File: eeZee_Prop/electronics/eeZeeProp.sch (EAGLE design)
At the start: 33 parts, among them Q1 5MHz, Q2 2N3904SMD, SW1 RESET, U1 P8X32A-Q44, U2 24LC256-I/ST, U3 NCP1117 3V3

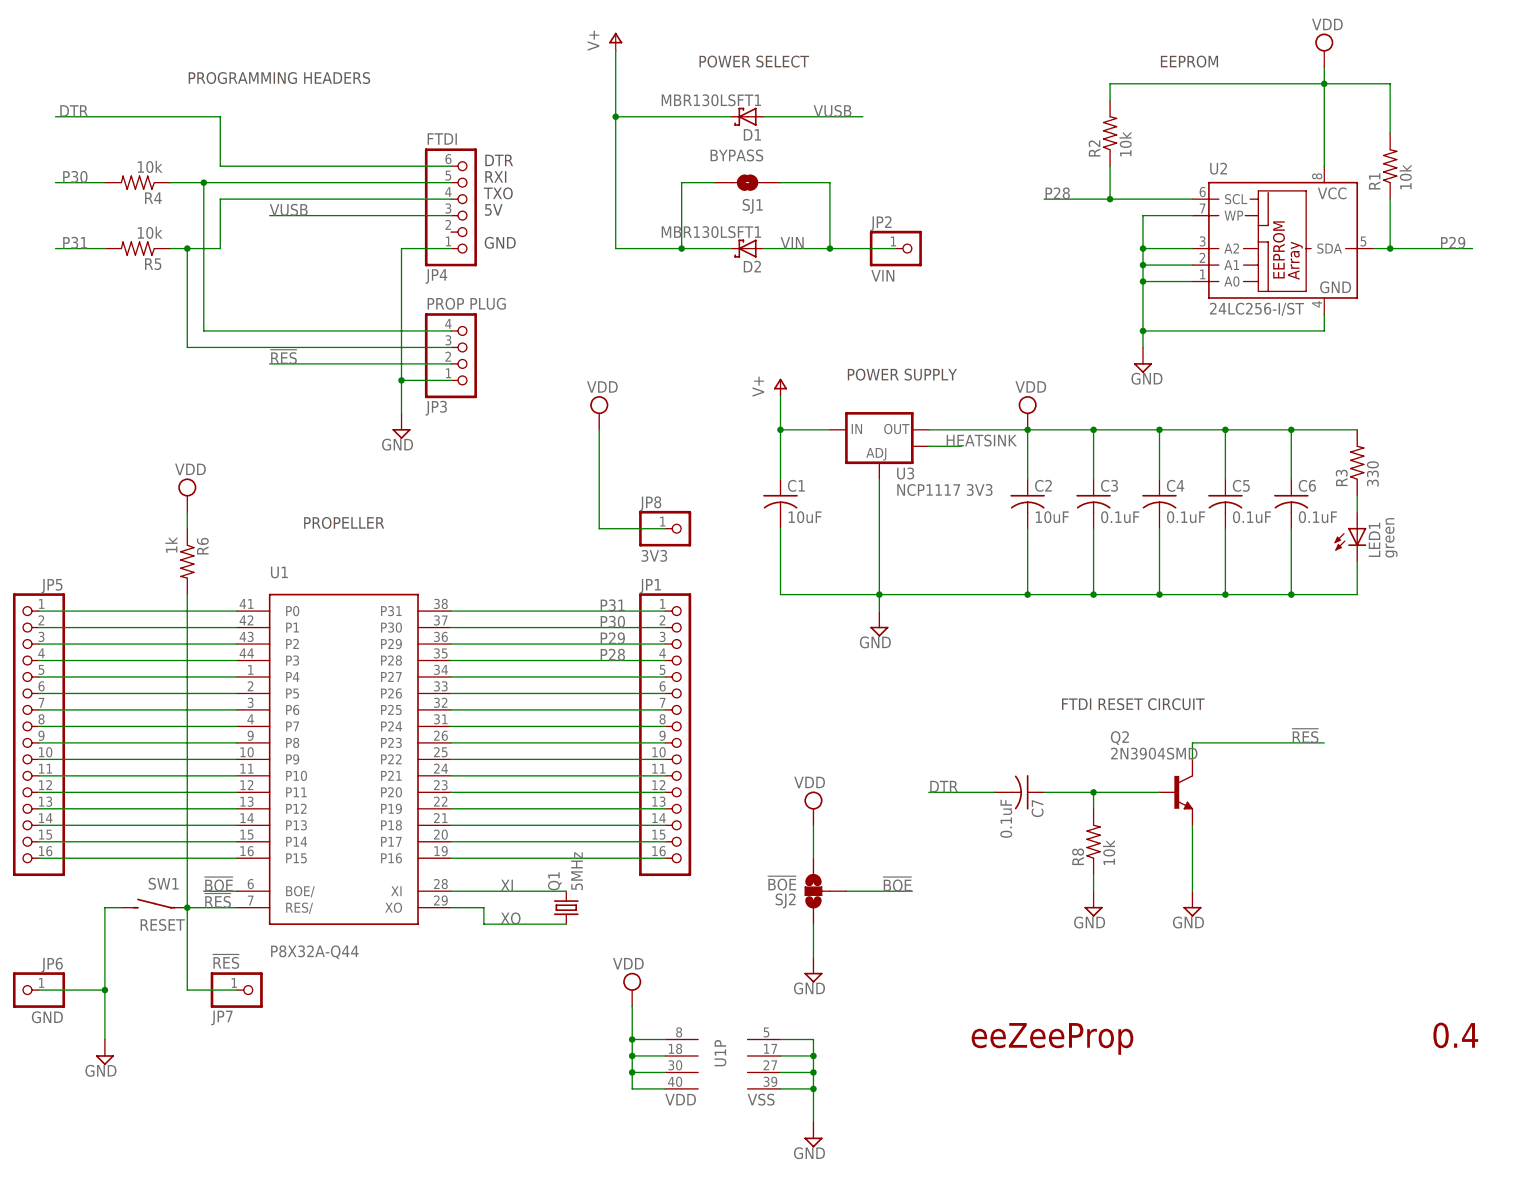
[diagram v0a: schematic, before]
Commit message: Added regulator bypass option for 3.3V FTDI. Increased diode pad sizes.
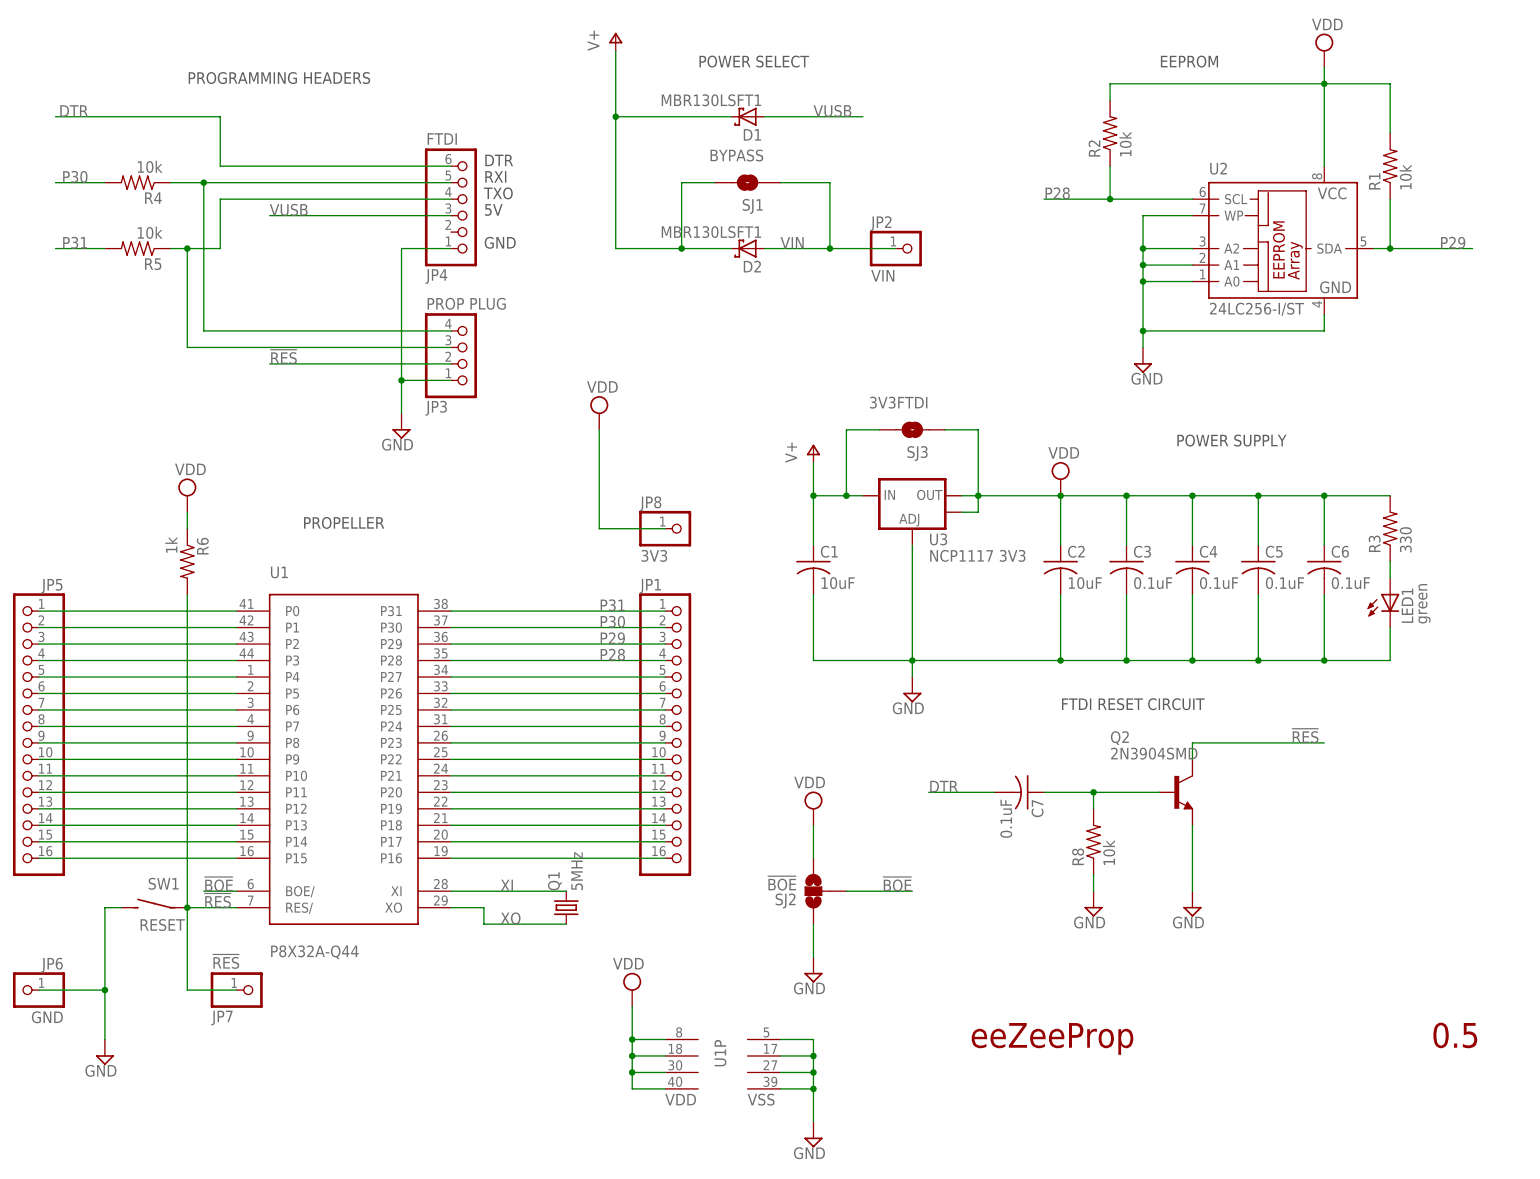
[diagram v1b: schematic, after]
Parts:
- added SJ3: 3V3FTDI, SparkFun:SOLDERJUMPERNO
- D1, D2: device mes_diode:SCHOTTKY-DIODE-MBR130LSFT1 -> bt_diode:SCHOTTKY-DIODE-MBR130LSFT1
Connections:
- removed net HEATSINK: U3.OUT@1
- net V+: now also SJ3.2
- net VDD: now also SJ3.1, U3.OUT@1
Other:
- note added: "0.5"
- note removed: "0.4"
- moved on the sheet: C1, C2, C3, C4, C5, C6, LED1, R3, U3

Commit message: Fixed silkscreen conflicts. Enlarged DTR/GND labels. Moved other silk labels to different layer, disabled bottom name silk gen.
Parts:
- Q2: device mes_transistors:2N3904SMD -> bt_transistor:2N3904SMD
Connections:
- net N$34 renamed RXI
- net N$35 renamed TXO
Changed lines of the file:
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@@
 </part>
 <part name="SJ1" library="SparkFun" deviceset="SOLDERJUMPER" device="NO" value="BYPASS"/>
-<part name="Q2" library="mes_transistors" deviceset="2N3904" device="SMD">
+<part name="Q2" library="bt_transistor" deviceset="2N3904" device="SMD">
 <attribute name="PARTNO" value="MMBT3904LT3G"/>
 </part>
@@
 </segment>
 </net>
-<net name="N$34" class="0">
+<net name="RXI" class="0">
 <segment>
 <pinref part="JP4" gate="A" pin="5"/>
@@
 </segment>
 </net>
-<net name="N$35" class="0">
+<net name="TXO" class="0">
 <segment>
 <pinref part="JP4" gate="A" pin="4"/>

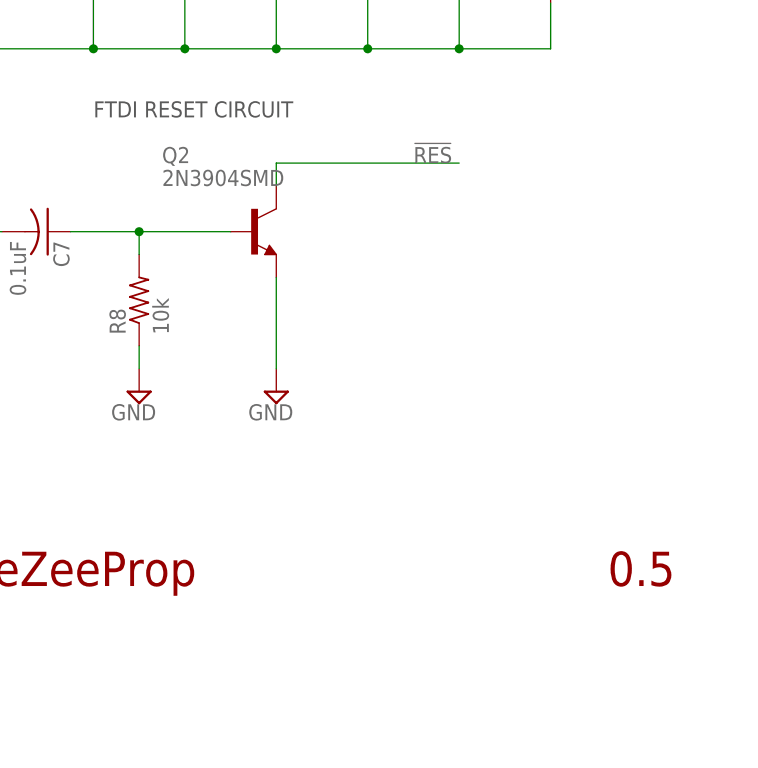
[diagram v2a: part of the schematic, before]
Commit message: Revised diode placement, silk, pin 1 dot on propeller.
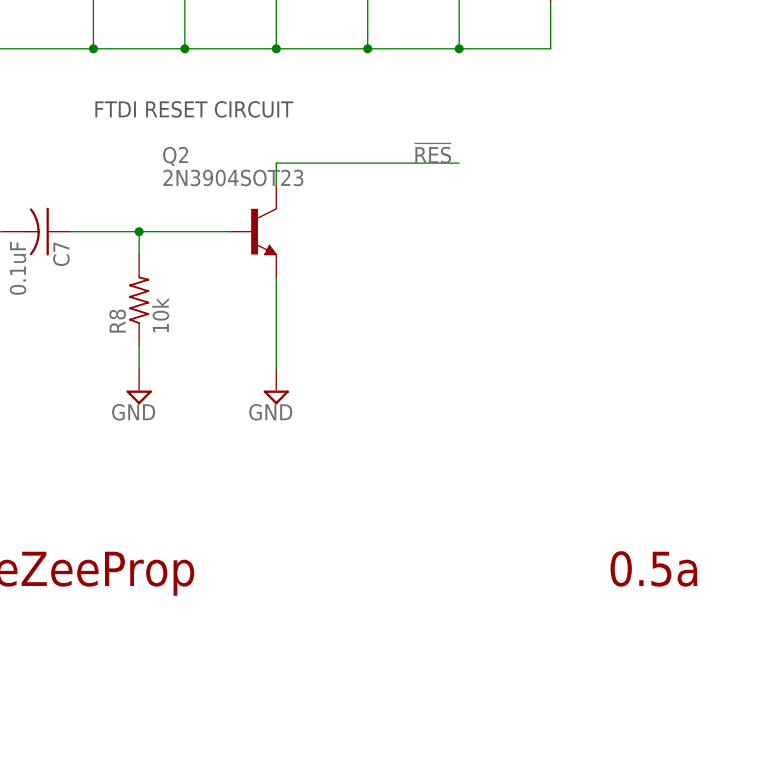
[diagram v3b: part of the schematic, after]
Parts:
- Q2: value 2N3904SMD -> 2N3904SOT23; device bt_transistor:2N3904SMD -> bt_transistor:2N3904SOT23
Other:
- note added: "0.5a"
- note removed: "0.5"
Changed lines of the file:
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@@
 </part>
 <part name="SJ1" library="SparkFun" deviceset="SOLDERJUMPER" device="NO" value="BYPASS"/>
-<part name="Q2" library="bt_transistor" deviceset="2N3904" device="SMD">
+<part name="Q2" library="bt_transistor" deviceset="2N3904" device="SOT23">
 <attribute name="PARTNO" value="MMBT3904LT3G"/>
 </part>
@@
 <text x="43.18" y="48.26" size="1.778" layer="95">!BOE</text>
 <text x="161.29" y="24.13" size="3.81" layer="94">eeZeeProp</text>
-<text x="232.41" y="24.13" size="3.81" layer="94">0.5</text>
+<text x="232.41" y="24.13" size="3.81" layer="94">0.5a</text>
 <text x="86.36" y="157.48" size="1.778" layer="97">RXI</text>
 <text x="86.36" y="154.94" size="1.778" layer="97">TXO</text>
